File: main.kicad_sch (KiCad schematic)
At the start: 15 parts, among them J1 Conn_02x16_Row_Letter_First

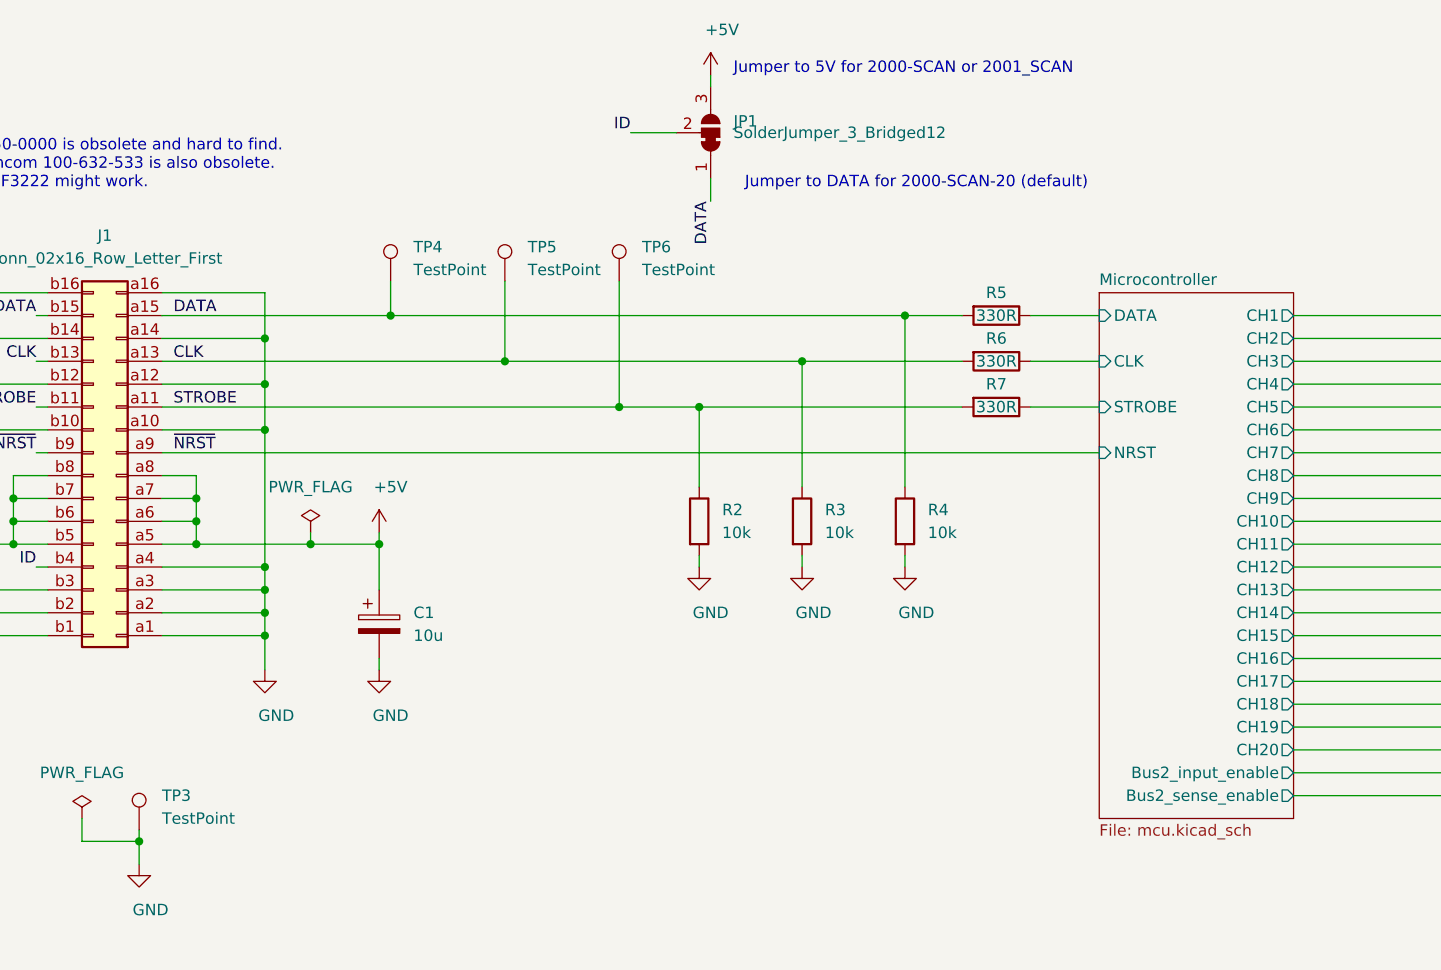
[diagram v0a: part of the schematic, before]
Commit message: Version 1.6
Created a high-voltage rated scan board.

Control is done completely in logic to avoid programming an MCU
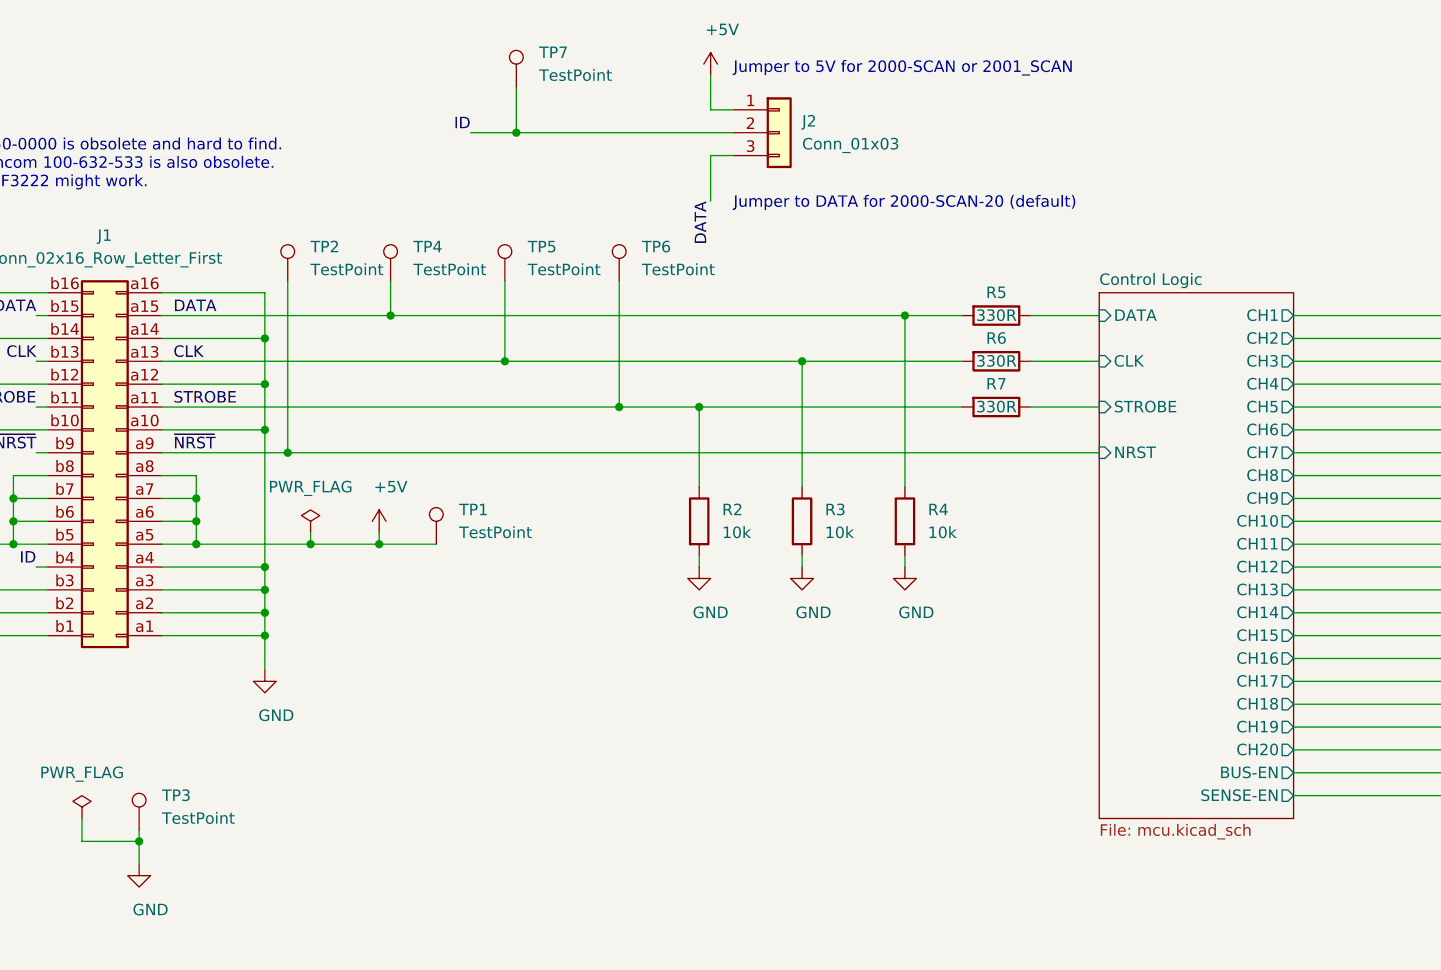
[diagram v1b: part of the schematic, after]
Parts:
- removed C1: 10u, Capacitor_THT:CP_Radial_D6.3mm_P2.50mm, symbol Device:C_Polarized
- removed JP1: SolderJumper_3_Bridged12, Jumper:SolderJumper-3_P1.3mm_Bridged12_Pad1.0x1.5mm_NumberLabels, symbol Jumper:SolderJumper_3_Bridged12
- added J2: Conn_01x03, Connector_PinHeader_2.54mm:PinHeader_1x03_P2.54mm_Vertical, symbol Connector_Generic:Conn_01x03
- added TP1, TP2, TP7: TestPoint, TestPoint:TestPoint_Loop_D2.60mm_Drill1.6mm_Beaded, symbol Connector:TestPoint
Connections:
- net +5V: now also J2.1 (Pin_1), TP1.1
- net DATA: now also J2.3 (Pin_3)
- net ID: now also J2.2 (Pin_2), TP7.1
- net ~{NRST}: now also TP2.1
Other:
- sheet Microcontroller renamed Control Logic
- sheet Control Logic ports: added BUS-EN, SENSE-EN; removed Bus2_input_enable, Bus2_sense_enable
